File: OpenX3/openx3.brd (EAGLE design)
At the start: 47 x 49.5 mm, 35 parts, among them IC1 24AA256SN, J1 BM20B-SRDS-G-TF(LF)(SN), J2 SM12B-SRSS-TB(LF)(SN), J3 53398-0271, J4 1734260-3, U1 LC4256V-75TN100CTQFP100-L, U2 AM29F016D-70EF, U3 AM29F002BB90EI

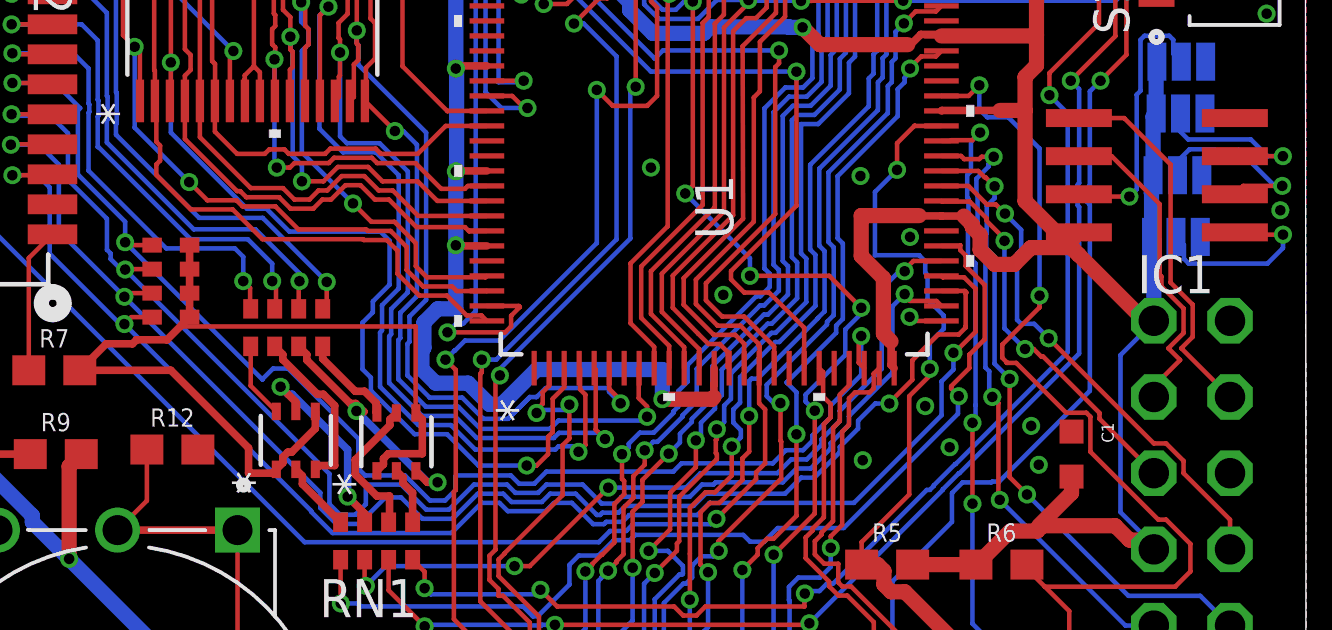
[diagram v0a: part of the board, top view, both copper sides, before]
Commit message: Make correction where resistor arrays were not connected to +3v3, previous net name was N$4 before connecting to +3v3
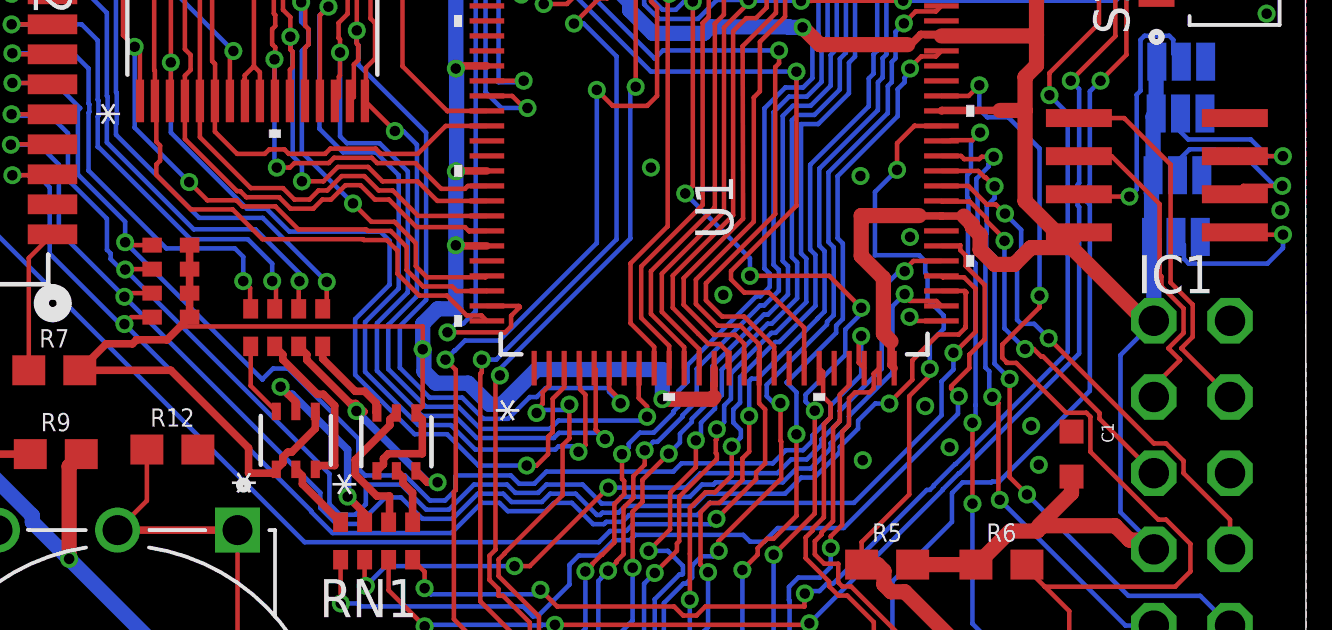
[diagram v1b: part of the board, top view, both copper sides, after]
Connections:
- removed net N$4: R3.1, R3.4, R4.1, R4.4, R7.2, RN2.1, RN2.2, RN2.3, RN2.4
- net +3V3: now also R3.1, R3.4, R4.1, R4.4, R7.2, RN2.1, RN2.2, RN2.3, RN2.4
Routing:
- net N$4: track 31.9 -> 0.00 mm
- net +3V3: track 153.1 -> 184.9 mm, vias 10 -> 11
- net A5: track 35.8 -> 35.0 mm

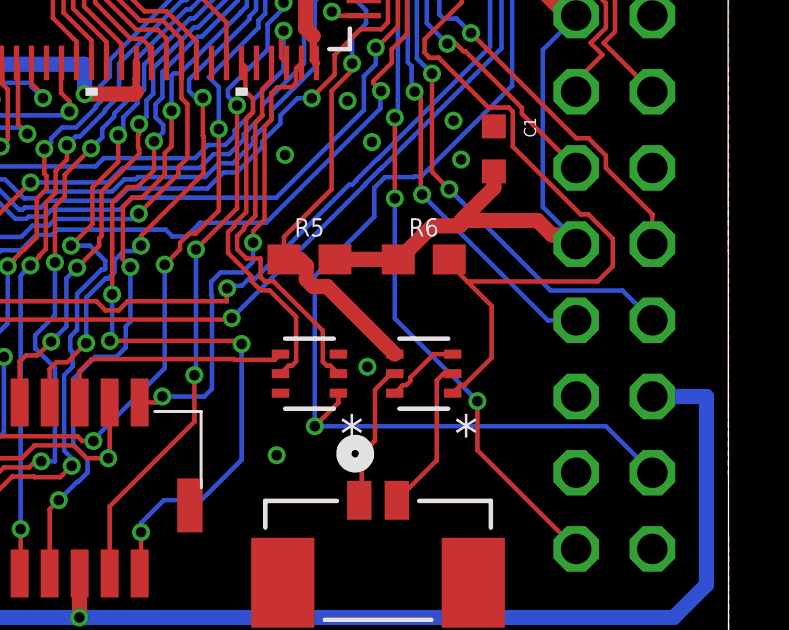
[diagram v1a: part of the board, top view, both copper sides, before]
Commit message: fixed missing ground connection to pins 3 and 6 of transistor array for front panel power and eject inputs
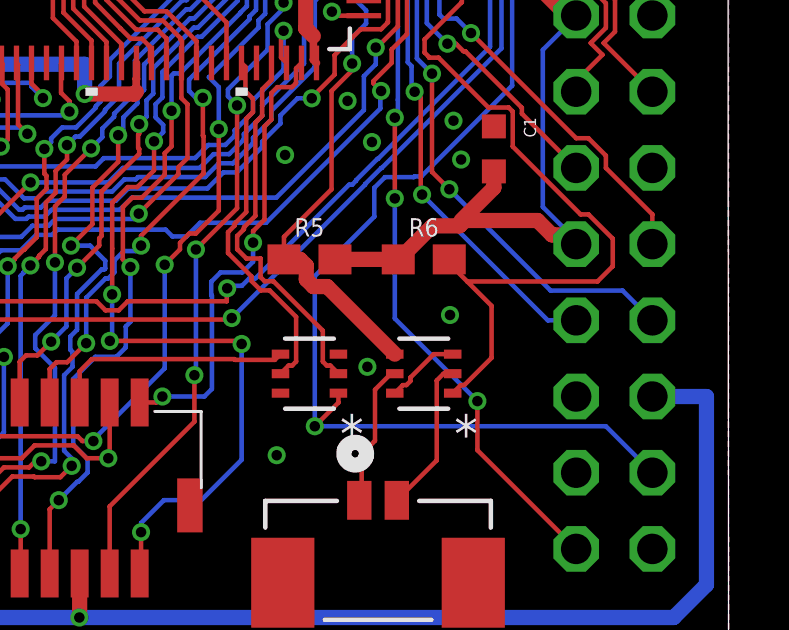
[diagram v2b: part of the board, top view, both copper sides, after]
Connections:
- removed net N$56: R1.3, R1.6
- net GND: now also R1.3, R1.6
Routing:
- net N$56: track 2.54 -> 0.00 mm
- net GND: track 1.12 -> 3.66 mm, vias 31 -> 32
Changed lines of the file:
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@@
 <wire x1="26.546525" y1="21.212525" x2="26.546525" y2="20.9376875" width="0.1524" layer="1"/>
-</signal>
-<signal name="N$56">
-<contactref element="R1" pad="3"/>
-<contactref element="R1" pad="6"/>
-<wire x1="35.8948" y1="8.27" x2="36.5252" y2="8.27" width="0.1524" layer="1"/>
-<wire x1="34.5948" y1="6.97" x2="34.8638" y2="7.239" width="0.1524" layer="1"/>
-<wire x1="34.8638" y1="7.239" x2="34.9815875" y2="7.239" width="0.1524" layer="1"/>
-<wire x1="34.9815875" y1="7.239" x2="35.1155" y2="7.3729125" width="0.1524" layer="1"/>
-<wire x1="35.1155" y1="7.3729125" x2="35.1155" y2="7.4907" width="0.1524" layer="1"/>
-<wire x1="35.1155" y1="7.4907" x2="35.8948" y2="8.27" width="0.1524" layer="1"/>
 </signal>
 <signal name="FPEJECT">
@@
 <via x="30.861" y="24.384" extent="1-16" drill="0.35"/>
 <via x="31.115" y="32.0294" extent="1-16" drill="0.35"/>
+<contactref element="R1" pad="3"/>
+<contactref element="R1" pad="6"/>
+<wire x1="35.8948" y1="8.27" x2="36.5252" y2="8.27" width="0.1524" layer="1"/>
+<wire x1="34.5948" y1="6.97" x2="34.8638" y2="7.239" width="0.1524" layer="1"/>
+<wire x1="34.8638" y1="7.239" x2="34.9815875" y2="7.239" width="0.1524" layer="1"/>
+<wire x1="34.9815875" y1="7.239" x2="35.1155" y2="7.3729125" width="0.1524" layer="1"/>
+<wire x1="35.1155" y1="7.3729125" x2="35.1155" y2="7.4907" width="0.1524" layer="1"/>
+<wire x1="35.1155" y1="7.4907" x2="35.8948" y2="8.27" width="0.1524" layer="1"/>
+<via x="36.434421875" y="9.575596875" extent="1-16" drill="0.35"/>
 </signal>
 <signal name="N$1">

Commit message: minor fixes to traces, but no changes, adding gerber file for 2nd pcb order with fixed 3v3 and gnd
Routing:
- net A1: track 56.3 -> 54.9 mm
- net A0: track 57.6 -> 56.3 mm
- net +3V3: track 184.9 -> 183.7 mm
- net A2: track 55.8 -> 54.8 mm
- net SWBANK3: track 47.8 -> 46.9 mm
- net DQ0: track 56.1 -> 55.2 mm
- net SWBANK4: track 48.1 -> 47.3 mm
- net DB0: track 54.7 -> 54.0 mm
- net A3: track 53.0 -> 52.3 mm
- net SWBANK1: track 44.3 -> 43.6 mm
- net SWBANK2: track 47.6 -> 47.0 mm
- net A16: track 38.7 -> 38.1 mm
- net DB7: track 29.3 -> 28.8 mm
- net TMS: track 46.4 -> 45.9 mm
- net N$78: track 32.7 -> 32.2 mm
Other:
- board text added: "OpenX3"

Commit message: Updated part # for mosfet array from Nch to Pch, possible replacement is SI1967DH-T1-GE3 but still waiting to verify. Also fixed error in DRC that cause solder mask to be missing around some components.
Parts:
- R1, R2, R3, R4: value UM6K31NFHATCNTRANS_UM6J1-L -> SI1967DH-T1-GE3
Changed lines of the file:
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@@
 </class>
 </classes>
-<designrules name="oshpark-2layer">
+<designrules name="oshpark-2layer *">
 <description language="en">&lt;b&gt;OSH Park Design Rules&lt;/b&gt;
 &lt;p&gt;
@@
 <param name="mvStopFrame" value="1"/>
 <param name="mvCreamFrame" value="0"/>
-<param name="mlMinStopFrame" value="2.5mil"/>
-<param name="mlMaxStopFrame" value="2.5mil"/>
+<param name="mlMinStopFrame" value="2mil"/>
+<param name="mlMaxStopFrame" value="2mil"/>
 <param name="mlMinCreamFrame" value="0mil"/>
 <param name="mlMaxCreamFrame" value="0mil"/>
-<param name="mlViaStopLimit" value="0mil"/>
+<param name="mlViaStopLimit" value="0.4mm"/>
 <param name="srRoundness" value="0"/>
 <param name="srMinRoundness" value="0mil"/>
@@
 <attribute name="VALUE" x="3.1496" y="15.5448" size="1.27" layer="27" rot="R90"/>
 </element>
-<element name="R1" library="UM6K31NFHA" package="TRANS_UM6J1-L" value="UM6K31NFHATCNTRANS_UM6J1-L" x="35.56" y="7.62" smashed="yes" rot="R180">
+<element name="R1" library="UM6K31NFHA" package="TRANS_UM6J1-L" value="SI1967DH-T1-GE3" x="35.56" y="7.62" smashed="yes" rot="R180">
 <attribute name="BUILT_BY" value="EMA_Matt" x="-31.75" y="74.93" size="1.778" layer="27" rot="R180" display="off"/>
 <attribute name="COPYRIGHT" value="Copyright (C) 2018 Accelerated Designs. All rights reserved" x="-31.75" y="74.93" size="1.778" layer="27" rot="R180" display="off"/>
@@
 <attribute name="VALUE" x="7.9248" y="14.5034" size="0.6096" layer="27" font="vector" ratio="20" align="top-center"/>
 </element>
-<element name="R2" library="UM6K31NFHA" package="TRANS_UM6J1-L" value="UM6K31NFHATCNTRANS_UM6J1-L" x="31.75" y="7.62" smashed="yes" rot="R180">
+<element name="R2" library="UM6K31NFHA" package="TRANS_UM6J1-L" value="SI1967DH-T1-GE3" x="31.75" y="7.62" smashed="yes" rot="R180">
 <attribute name="BUILT_BY" value="EMA_Matt" x="-10.16" y="80.01" size="1.778" layer="27" rot="R180" display="off"/>
 <attribute name="COPYRIGHT" value="Copyright (C) 2018 Accelerated Designs. All rights reserved" x="-10.16" y="80.01" size="1.778" layer="27" rot="R180" display="off"/>
@@
 <attribute name="VENDOR" value="ROHM Semiconductor" x="-10.16" y="80.01" size="1.778" layer="27" rot="R180" display="off"/>
 </element>
-<element name="R3" library="UM6K31NFHA" package="TRANS_UM6J1-L" value="UM6K31NFHATCNTRANS_UM6J1-L" x="15.3924" y="15.5194" smashed="yes" rot="R90">
+<element name="R3" library="UM6K31NFHA" package="TRANS_UM6J1-L" value="SI1967DH-T1-GE3" x="15.3924" y="15.5194" smashed="yes" rot="R90">
 <attribute name="BUILT_BY" value="EMA_Matt" x="87.7824" y="90.4494" size="1.778" layer="27" rot="R90" display="off"/>
 <attribute name="COPYRIGHT" value="Copyright (C) 2018 Accelerated Designs. All rights reserved" x="87.7824" y="90.4494" size="1.778" layer="27" rot="R90" display="off"/>
@@
 <attribute name="VENDOR" value="ROHM Semiconductor" x="87.7824" y="90.4494" size="1.778" layer="27" rot="R90" display="off"/>
 </element>
-<element name="R4" library="UM6K31NFHA" package="TRANS_UM6J1-L" value="UM6K31NFHATCNTRANS_UM6J1-L" x="12.0396" y="15.5702" smashed="yes" rot="R90">
+<element name="R4" library="UM6K31NFHA" package="TRANS_UM6J1-L" value="SI1967DH-T1-GE3" x="12.0396" y="15.5702" smashed="yes" rot="R90">
 <attribute name="BUILT_BY" value="EMA_Matt" x="89.5096" y="57.4802" size="1.778" layer="27" rot="R90" display="off"/>
 <attribute name="COPYRIGHT" value="Copyright (C) 2018 Accelerated Designs. All rights reserved" x="89.5096" y="57.4802" size="1.778" layer="27" rot="R90" display="off"/>
